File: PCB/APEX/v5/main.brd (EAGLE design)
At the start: 38.1 x 38.1 mm, 5 parts

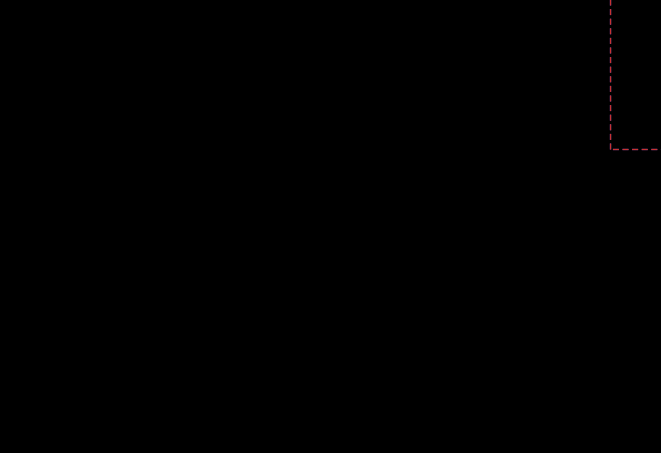
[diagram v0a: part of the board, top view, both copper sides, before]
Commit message: add STM 1n5819 to schematic
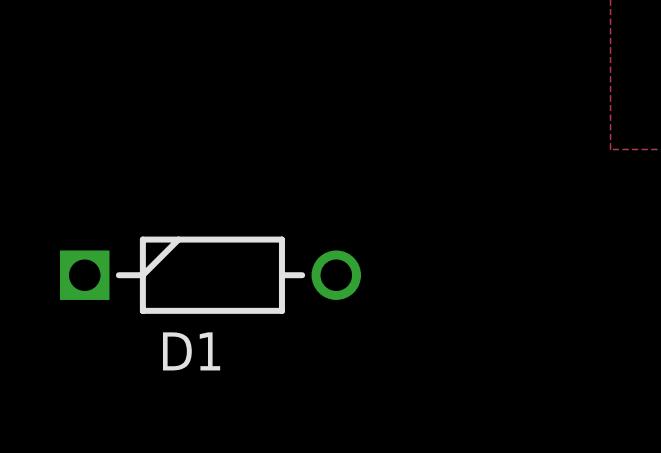
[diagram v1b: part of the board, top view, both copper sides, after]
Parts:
- added D1: 1N5819, SamacSys_Parts:DIOAD1414W86L464D238
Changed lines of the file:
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@@
 <layer number="19" name="Unrouted" color="6" fill="1" visible="yes" active="yes"/>
 <layer number="20" name="Dimension" color="24" fill="1" visible="yes" active="yes"/>
-<layer number="21" name="tPlace" color="16" fill="1" visible="no" active="yes"/>
+<layer number="21" name="tPlace" color="16" fill="1" visible="yes" active="yes"/>
 <layer number="22" name="bPlace" color="14" fill="1" visible="yes" active="yes"/>
 <layer number="23" name="tOrigins" color="15" fill="1" visible="yes" active="yes"/>
@@
 <layer number="29" name="tStop" color="7" fill="3" visible="yes" active="yes"/>
 <layer number="30" name="bStop" color="7" fill="6" visible="yes" active="yes"/>
-<layer number="31" name="tCream" color="7" fill="4" visible="yes" active="yes"/>
-<layer number="32" name="bCream" color="7" fill="5" visible="yes" active="yes"/>
-<layer number="33" name="tFinish" color="6" fill="3" visible="yes" active="yes"/>
-<layer number="34" name="bFinish" color="6" fill="6" visible="yes" active="yes"/>
-<layer number="35" name="tGlue" color="7" fill="4" visible="yes" active="yes"/>
-<layer number="36" name="bGlue" color="7" fill="5" visible="yes" active="yes"/>
-<layer number="37" name="tTest" color="7" fill="1" visible="yes" active="yes"/>
-<layer number="38" name="bTest" color="7" fill="1" visible="yes" active="yes"/>
-<layer number="39" name="tKeepout" color="4" fill="11" visible="yes" active="yes"/>
-<layer number="40" name="bKeepout" color="1" fill="11" visible="yes" active="yes"/>
-<layer number="41" name="tRestrict" color="4" fill="10" visible="yes" active="yes"/>
-<layer number="42" name="bRestrict" color="1" fill="10" visible="yes" active="yes"/>
-<layer number="43" name="vRestrict" color="2" fill="10" visible="yes" active="yes"/>
+<layer number="31" name="tCream" color="7" fill="4" visible="no" active="yes"/>
+<layer number="32" name="bCream" color="7" fill="5" visible="no" active="yes"/>
+<layer number="33" name="tFinish" color="6" fill="3" visible="no" active="yes"/>
+<layer number="34" name="bFinish" color="6" fill="6" visible="no" active="yes"/>
+<layer number="35" name="tGlue" color="7" fill="4" visible="no" active="yes"/>
+<layer number="36" name="bGlue" color="7" fill="5" visible="no" active="yes"/>
+<layer number="37" name="tTest" color="7" fill="1" visible="no" active="yes"/>
+<layer number="38" name="bTest" color="7" fill="1" visible="no" active="yes"/>
+<layer number="39" name="tKeepout" color="4" fill="11" visible="no" active="yes"/>
+<layer number="40" name="bKeepout" color="1" fill="11" visible="no" active="yes"/>
+<layer number="41" name="tRestrict" color="4" fill="10" visible="no" active="yes"/>
+<layer number="42" name="bRestrict" color="1" fill="10" visible="no" active="yes"/>
+<layer number="43" name="vRestrict" color="2" fill="10" visible="no" active="yes"/>
 <layer number="44" name="Drills" color="7" fill="1" visible="yes" active="yes"/>
 <layer number="45" name="Holes" color="7" fill="1" visible="yes" active="yes"/>
-<layer number="46" name="Milling" color="3" fill="1" visible="yes" active="yes"/>
-<layer number="47" name="Measures" color="7" fill="1" visible="yes" active="yes"/>
-<layer number="48" name="Document" color="7" fill="1" visible="yes" active="yes"/>
-<layer number="49" name="Reference" color="7" fill="1" visible="yes" active="yes"/>
+<layer number="46" name="Milling" color="3" fill="1" visible="no" active="yes"/>
+<layer number="47" name="Measures" color="7" fill="1" visible="no" active="yes"/>
+<layer number="48" name="Document" color="7" fill="1" visible="no" active="yes"/>
+<layer number="49" name="Reference" color="7" fill="1" visible="no" active="yes"/>
 <layer number="50" name="dxf" color="7" fill="1" visible="no" active="no"/>
 <layer number="51" name="tDocu" color="6" fill="1" visible="yes" active="yes"/>
@@
 <attribute name="VALUE" x="-6.2865" y="-10.16" size="0.4064" layer="27" ratio="10"/>
 </element>
+<element name="D1" library="SamacSys_Parts" package="DIOAD1414W86L464D238" value="1N5819" x="-43.18" y="-27.051" smashed="yes">
+<attribute name="ALLIED_NUMBER" value="70013816" x="-43.18" y="-27.051" size="1.778" layer="27" font="vector" ratio="15" display="off"/>
+<attribute name="DESCRIPTION" value="Schottky barrier diode,1N58191A 40V STMicroelectronics 1N5819, Schottky Diode, 40V 1A, 2-Pin DO-204AL" x="-43.18" y="-27.051" size="1.778" layer="27" font="vector" ratio="15" display="off"/>
+<attribute name="HEIGHT" value="mm" x="-43.18" y="-27.051" size="1.778" layer="27" font="vector" ratio="15" display="off"/>
+<attribute name="MANUFACTURER_NAME" value="STMicroelectronics" x="-43.18" y="-27.051" size="1.778" layer="27" font="vector" ratio="15" display="off"/>
+<attribute name="MANUFACTURER_PART_NUMBER" value="1N5819" x="-43.18" y="-27.051" size="1.778" layer="27" font="vector" ratio="15" display="off"/>
+<attribute name="NAME" x="-36.83" y="-29.590996875" size="1.27" layer="25" align="center"/>
+<attribute name="RS_PART_NUMBER" value="4864460P" x="-43.18" y="-27.051" size="1.778" layer="27" font="vector" ratio="15" display="off"/>
+<attribute name="RS_PRICE-STOCK" value="http://uk.rs-online.com/web/p/products/4864460P" x="-43.18" y="-27.051" size="1.778" layer="27" font="vector" ratio="15" display="off"/>
+<attribute name="VALUE" x="-36.83" y="-24.510996875" size="1.27" layer="27" align="center"/>
+</element>
 </elements>

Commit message: connect schottky
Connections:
- new net VBAT: CN1.1, D1.2
- net VCC: now also D1.1; no longer CN1.1
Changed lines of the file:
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@@
 <signal name="VCC">
 <contactref element="JP2" pad="2"/>
-<contactref element="CN1" pad="1"/>
 <polygon width="1.016" layer="1" isolate="0.508">
 <vertex x="-22.86" y="21.59"/>
@@
 <wire x1="10.2235" y1="-6.985" x2="10.2235" y2="-8.4455" width="1.524" layer="1"/>
 <wire x1="10.2235" y1="-8.4455" x2="10.16" y2="-8.509" width="1.524" layer="1"/>
+<contactref element="D1" pad="1"/>
+<wire x1="-11.176" y1="3.175" x2="-40.386" y2="-27.051" width="0" layer="19" extent="1-1"/>
+<wire x1="2.54" y1="14.605" x2="-11.176" y2="3.175" width="0" layer="19" extent="1-1"/>
+<wire x1="10.2235" y1="-6.985" x2="2.54" y2="14.605" width="0" layer="19" extent="1-1"/>
 </signal>
 <signal name="GND">
@@
 <wire x1="10.287" y1="9.271" x2="10.287" y2="9.525" width="1.524" layer="1"/>
 </signal>
+<signal name="VBAT">
+<contactref element="CN1" pad="1"/>
+<contactref element="D1" pad="2"/>
+<wire x1="-4.81" y1="-13.97" x2="-32.001" y2="-27.051" width="0" layer="19" extent="1-1"/>
+</signal>
 </signals>

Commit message: place diode on pcb
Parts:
- moved D1 37.3 mm to (-9.27, -11.4), turned to 330 degrees
- moved CN1 8.89 mm to (5.08, -14.0)
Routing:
- net VBAT: track 0.00 -> 4.93 mm
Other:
- board text added: "D+"
- board text added: "D-"

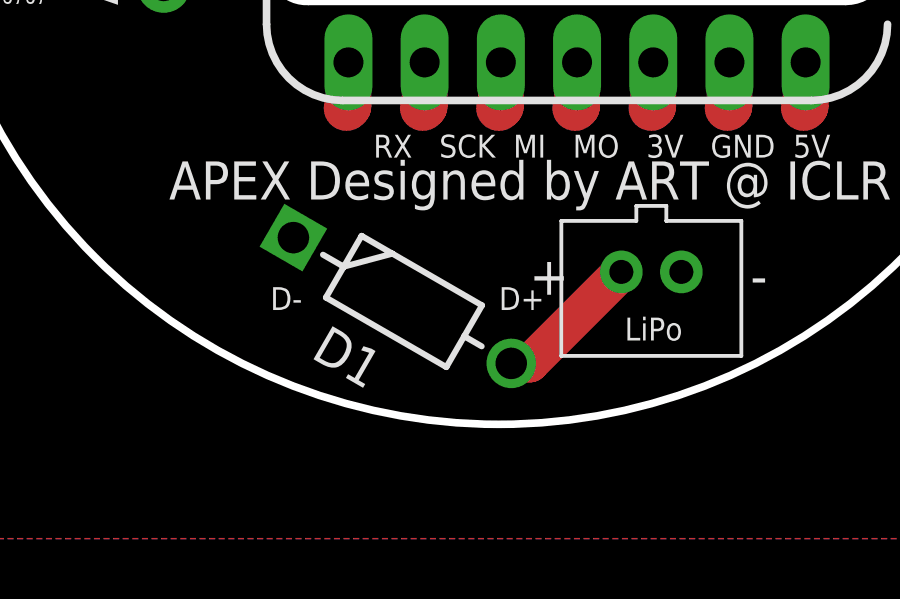
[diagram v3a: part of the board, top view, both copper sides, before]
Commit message: shuffle diode to keep logo plated
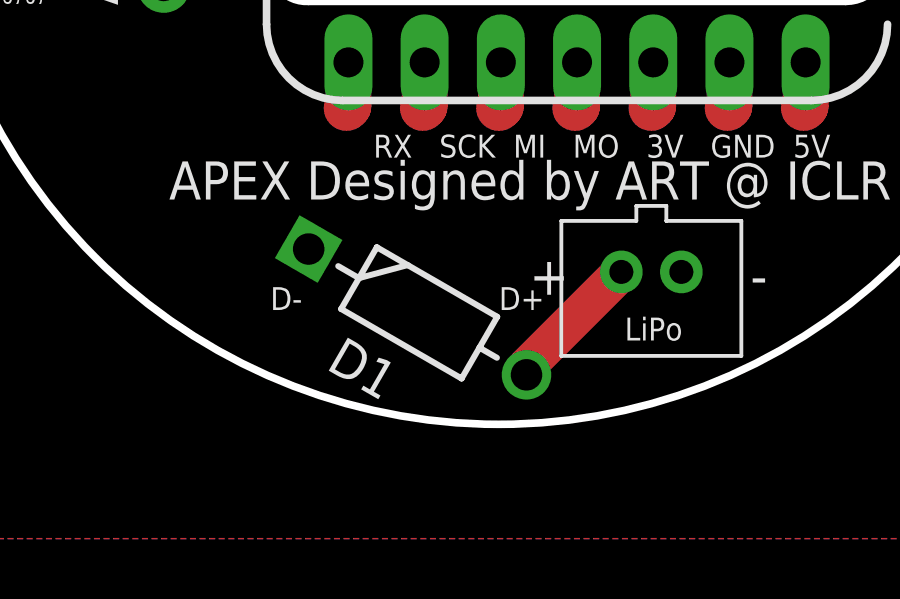
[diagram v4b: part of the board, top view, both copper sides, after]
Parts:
- moved D1 0.64 mm to (-8.76, -11.8)
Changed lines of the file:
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@@
 <attribute name="VALUE" x="-6.2865" y="-10.16" size="0.4064" layer="27" ratio="10"/>
 </element>
-<element name="D1" library="SamacSys_Parts" package="DIOAD1414W86L464D238" value="1N5819" x="-9.271" y="-11.43" smashed="yes" rot="R330">
-<attribute name="ALLIED_NUMBER" value="70013816" x="-9.271" y="-11.43" size="1.778" layer="27" font="vector" ratio="15" rot="R330" display="off"/>
-<attribute name="DESCRIPTION" value="Schottky barrier diode,1N58191A 40V STMicroelectronics 1N5819, Schottky Diode, 40V 1A, 2-Pin DO-204AL" x="-9.271" y="-11.43" size="1.778" layer="27" font="vector" ratio="15" rot="R330" display="off"/>
-<attribute name="HEIGHT" value="mm" x="-9.271" y="-11.43" size="1.778" layer="27" font="vector" ratio="15" rot="R330" display="off"/>
-<attribute name="MANUFACTURER_NAME" value="STMicroelectronics" x="-9.271" y="-11.43" size="1.778" layer="27" font="vector" ratio="15" rot="R330" display="off"/>
-<attribute name="MANUFACTURER_PART_NUMBER" value="1N5819" x="-9.271" y="-11.43" size="1.778" layer="27" font="vector" ratio="15" rot="R330" display="off"/>
-<attribute name="NAME" x="-5.0417375" y="-16.8047" size="1.27" layer="25" rot="R330" align="center"/>
-<attribute name="RS_PART_NUMBER" value="4864460P" x="-9.271" y="-11.43" size="1.778" layer="27" font="vector" ratio="15" rot="R330" display="off"/>
-<attribute name="RS_PRICE-STOCK" value="http://uk.rs-online.com/web/p/products/4864460P" x="-9.271" y="-11.43" size="1.778" layer="27" font="vector" ratio="15" rot="R330" display="off"/>
+<element name="D1" library="SamacSys_Parts" package="DIOAD1414W86L464D238" value="1N5819" x="-8.763" y="-11.811" smashed="yes" rot="R330">
+<attribute name="ALLIED_NUMBER" value="70013816" x="-8.763" y="-11.811" size="1.778" layer="27" font="vector" ratio="15" rot="R330" display="off"/>
+<attribute name="DESCRIPTION" value="Schottky barrier diode,1N58191A 40V STMicroelectronics 1N5819, Schottky Diode, 40V 1A, 2-Pin DO-204AL" x="-8.763" y="-11.811" size="1.778" layer="27" font="vector" ratio="15" rot="R330" display="off"/>
+<attribute name="HEIGHT" value="mm" x="-8.763" y="-11.811" size="1.778" layer="27" font="vector" ratio="15" rot="R330" display="off"/>
+<attribute name="MANUFACTURER_NAME" value="STMicroelectronics" x="-8.763" y="-11.811" size="1.778" layer="27" font="vector" ratio="15" rot="R330" display="off"/>
+<attribute name="MANUFACTURER_PART_NUMBER" value="1N5819" x="-8.763" y="-11.811" size="1.778" layer="27" font="vector" ratio="15" rot="R330" display="off"/>
+<attribute name="NAME" x="-4.5337375" y="-17.1857" size="1.27" layer="25" rot="R330" align="center"/>
+<attribute name="RS_PART_NUMBER" value="4864460P" x="-8.763" y="-11.811" size="1.778" layer="27" font="vector" ratio="15" rot="R330" display="off"/>
+<attribute name="RS_PRICE-STOCK" value="http://uk.rs-online.com/web/p/products/4864460P" x="-8.763" y="-11.811" size="1.778" layer="27" font="vector" ratio="15" rot="R330" display="off"/>
 </element>
 </elements>
@@
 <contactref element="CN1" pad="1"/>
 <contactref element="D1" pad="2"/>
-<wire x1="4.08" y1="-13.97" x2="1.0305" y2="-17.0195" width="1.27" layer="1"/>
-<wire x1="1.0305" y1="-17.0195" x2="0.410296875" y2="-17.0195" width="1.27" layer="1"/>
+<wire x1="4.08" y1="-13.97" x2="0.918296875" y2="-17.131703125" width="1.27" layer="1"/>
+<wire x1="0.918296875" y1="-17.131703125" x2="0.918296875" y2="-17.4005" width="1.27" layer="1"/>
 </signal>
 </signals>
